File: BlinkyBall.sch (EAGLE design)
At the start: 23 parts, among them J1 M02PTH, U1 Tiny85-20-SMT

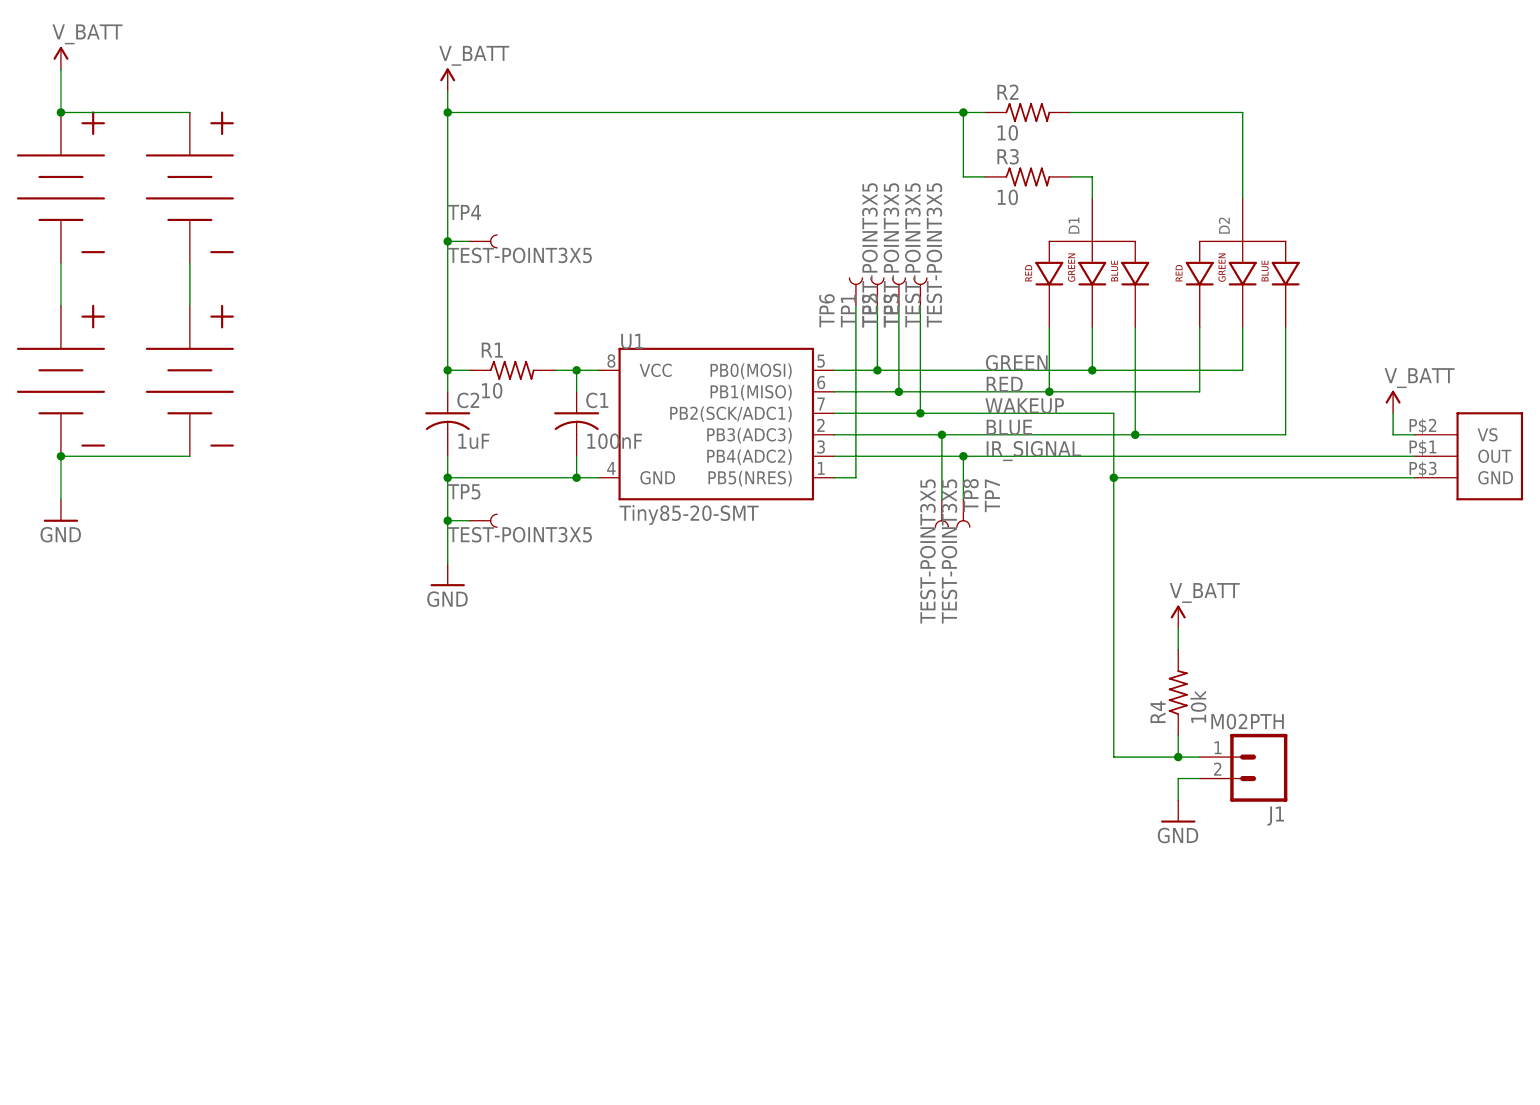
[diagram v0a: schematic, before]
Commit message: Working towards RevB board design: Smaller, more vertical
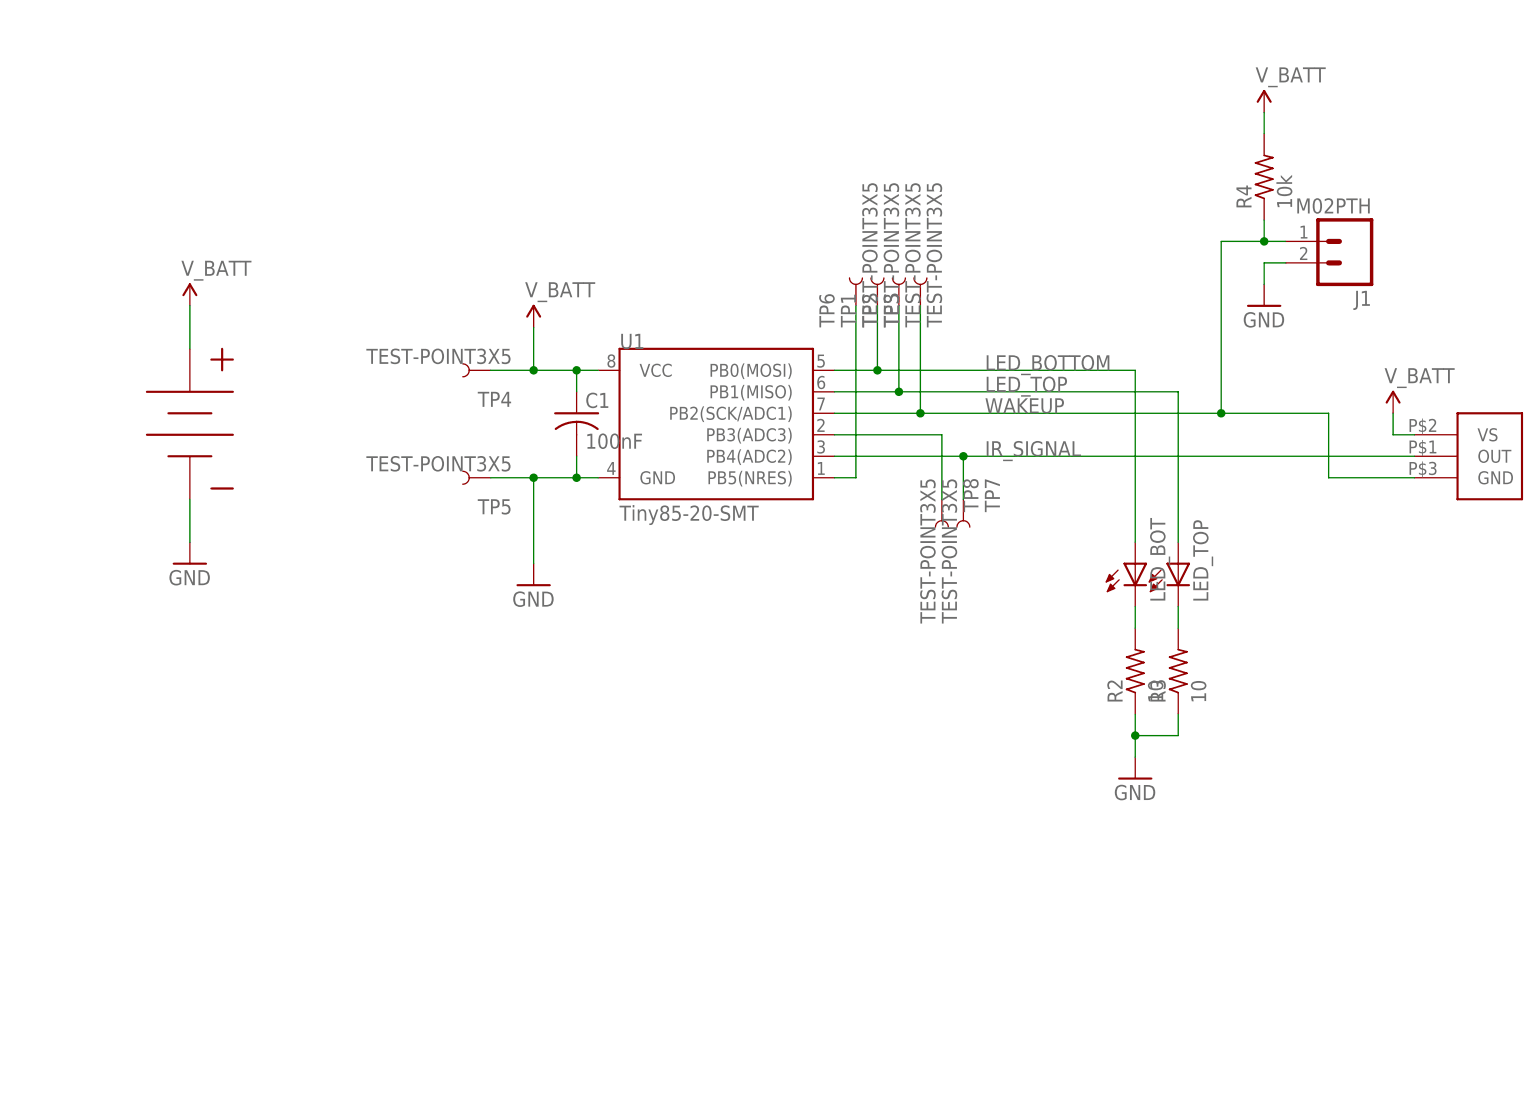
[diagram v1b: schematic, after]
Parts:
- removed C2: 1uF, adafruit:C-USC0603
- removed D1, D2: LED-RGB-CA-THRUDIFFUSE, blinkinlabs:LED-RGB-CA-THRUDIFFUSE
- removed R1: 10, adafruit:R-US_R0603
- removed U$1, U$3, U$4: BATTERY_BUTTON_CELLAG3-REVERSABLE, blinkinlabs:BATTERY_BUTTON_CELLAG3-REVERSABLE
- added LED_BOT, LED_TOP: (no value), adafruit:LED5MM
- U$2: value BATTERY_BUTTON_CELLAG3-REVERSABLE -> BATTERY_BUTTON_CELLAG3; device blinkinlabs:BATTERY_BUTTON_CELLAG3-REVERSABLE -> blinkinlabs:BATTERY_BUTTON_CELLAG3
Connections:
- net N$4 renamed RESET
- removed net BLUE: D1.BLUE_CATHODE, D2.BLUE_CATHODE, TP8.1, U1.PB3(ADC3)
- removed net GREEN: D1.GREEN_CATHODE, D2.GREEN_CATHODE, TP1.1, U1.PB0(MOSI)
- removed net N$1: U$1.-, U$2.+
- removed net N$2: U$3.-, U$4.+
- removed net N$3: C1.1, R1.2, U1.VCC
- removed net N$8: D2.ANODE, R2.2
- removed net N$9: D1.ANODE, R3.2
- removed net RED: D1.RED_CATHODE, D2.RED_CATHODE, TP2.1, U1.PB1(MISO)
- new net LED_BOTTOM: LED_BOT.A, TP1.1, U1.PB0(MOSI)
- new net LED_TOP: LED_TOP.A, TP2.1, U1.PB1(MISO)
- new net N$4: LED_TOP.C, R3.2
- new net N$5: LED_BOT.C, R2.2
- new net XXXXX: TP8.1, U1.PB3(ADC3)
- net GND: now also R2.1, R3.1; no longer C2.2, U$4.-
- net V_BATT: now also C1.1, U$2.+, U1.VCC; no longer C2.1, R1.1, R2.1, R3.1, U$1.+, U$3.+
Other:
- moved on the sheet: J1, R2, R3, R4, TP4, TP5

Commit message: RevB pcb- transistor switch for LEDs
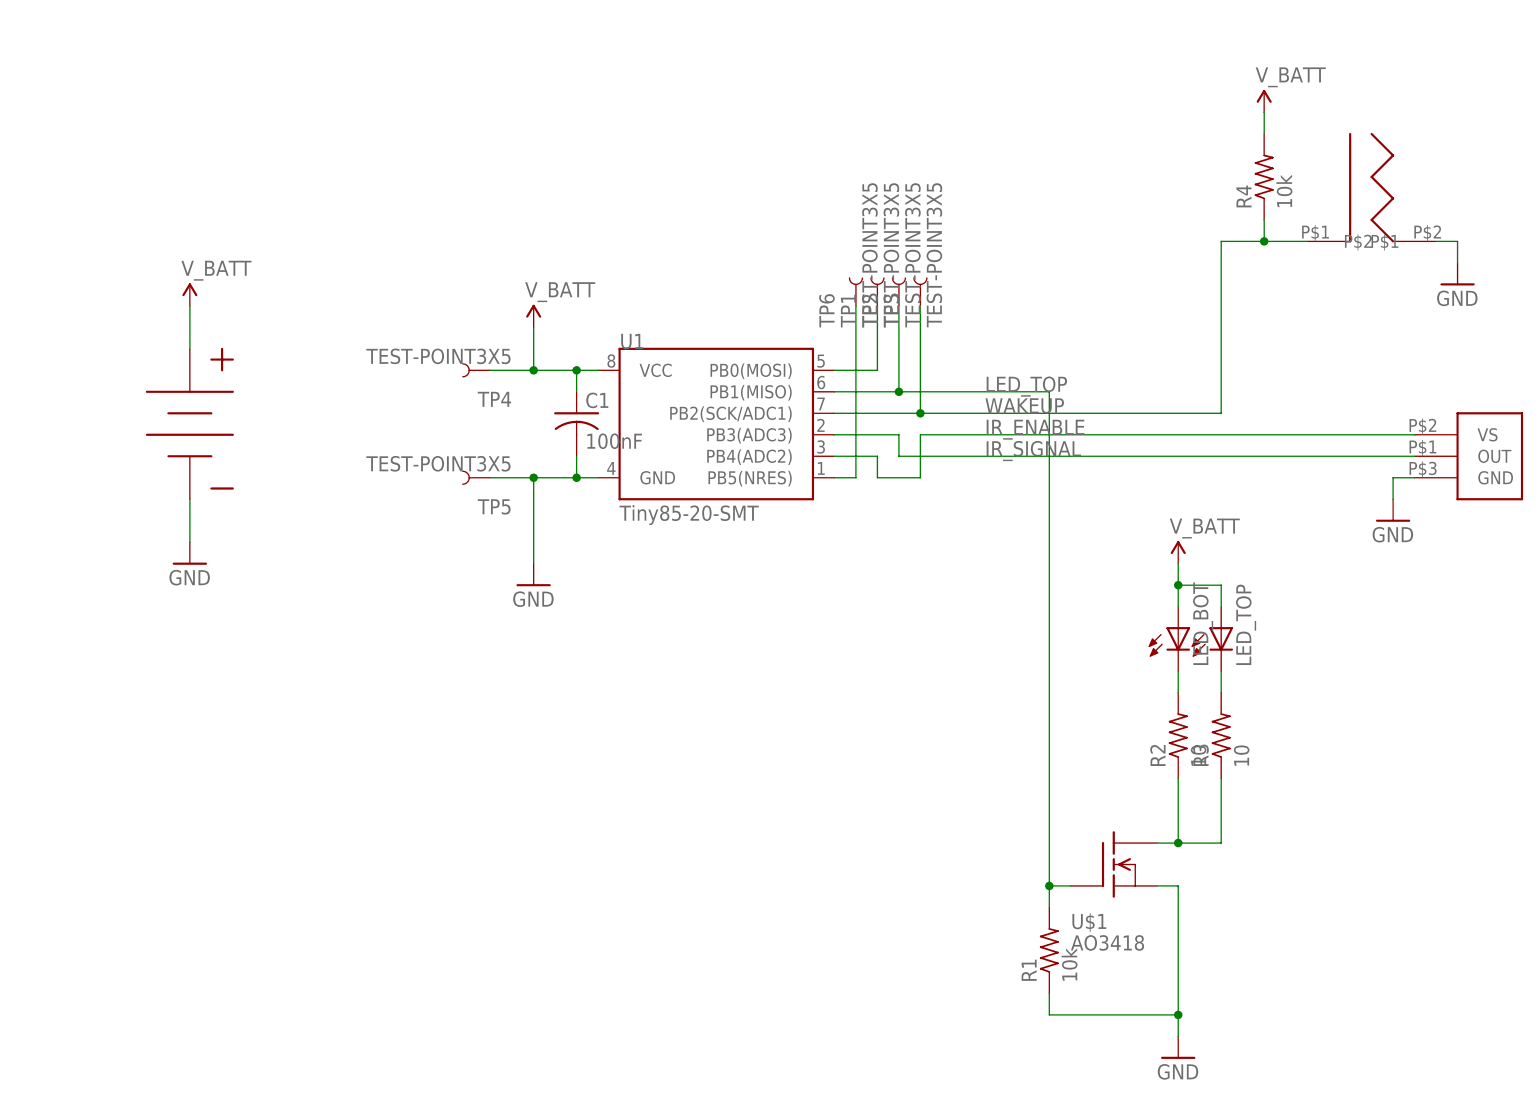
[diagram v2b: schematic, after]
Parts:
- removed J1: M02PTH, SparkFun-Connectors:M02PTH
- removed TP7, TP8: TEST-POINT3X5, SparkFun-Passives:TEST-POINT3X5
- added R1: 10k, adafruit:R-US_R0603
- added U$1: AO3418, blinkinlabs:N_MOSFETSOT23
- added U$3: SW-18015P, blinkinlabs:SW-18015P
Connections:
- removed net LED_BOTTOM: LED_BOT.A, TP1.1, U1.PB0(MOSI)
- removed net XXXXX: TP8.1, U1.PB3(ADC3)
- new net IR_ENABLE: U$5.VS, U1.PB4(ADC2)
- new net N$4: R2.1, R3.1, U$1.D
- new net YYYYY: TP1.1, U1.PB0(MOSI)
- net GND: now also R1.1, U$1.S, U$3.P$2, U$5.GND; no longer J1.2, R2.1, R3.1
- net IR_SIGNAL: now also U1.PB3(ADC3); no longer TP7.1, U1.PB4(ADC2)
- net LED_TOP: now also R1.2, U$1.G; no longer LED_TOP.A
- net V_BATT: now also LED_BOT.A, LED_TOP.A; no longer U$5.VS
- net WAKEUP: now also U$3.P$1; no longer J1.1, U$5.GND
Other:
- moved on the sheet: LED_BOT, LED_TOP, R2, R3
